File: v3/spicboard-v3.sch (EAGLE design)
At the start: 40 parts, among them IC1 74HC595, Q1 BC557, Q2 BC557

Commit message: SPiCboard...
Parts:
- C1, C2: device spicboard-v3:C2.5/2 -> capacitor-wima:C2.5/2
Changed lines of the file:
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@@
 <grid distance="0.1" unitdist="inch" unit="inch" style="lines" multiple="1" display="no" altdistance="0.01" altunitdist="inch" altunit="inch"/>
 <layers>
-<layer number="1" name="Top" color="4" fill="1" visible="yes" active="no"/>
-<layer number="16" name="Bottom" color="1" fill="1" visible="yes" active="no"/>
-<layer number="17" name="Pads" color="2" fill="1" visible="yes" active="no"/>
-<layer number="18" name="Vias" color="2" fill="1" visible="yes" active="no"/>
-<layer number="19" name="Unrouted" color="6" fill="1" visible="yes" active="no"/>
-<layer number="20" name="Dimension" color="15" fill="1" visible="yes" active="no"/>
-<layer number="21" name="tPlace" color="7" fill="1" visible="yes" active="no"/>
-<layer number="22" name="bPlace" color="7" fill="1" visible="yes" active="no"/>
-<layer number="23" name="tOrigins" color="15" fill="1" visible="yes" active="no"/>
-<layer number="24" name="bOrigins" color="15" fill="1" visible="yes" active="no"/>
-<layer number="25" name="tNames" color="7" fill="1" visible="yes" active="no"/>
-<layer number="26" name="bNames" color="7" fill="1" visible="yes" active="no"/>
-<layer number="27" name="tValues" color="7" fill="1" visible="yes" active="no"/>
-<layer number="28" name="bValues" color="7" fill="1" visible="yes" active="no"/>
+<layer number="1" name="Top" color="4" fill="1" visible="no" active="no"/>
+<layer number="16" name="Bottom" color="1" fill="1" visible="no" active="no"/>
+<layer number="17" name="Pads" color="2" fill="1" visible="no" active="no"/>
+<layer number="18" name="Vias" color="2" fill="1" visible="no" active="no"/>
+<layer number="19" name="Unrouted" color="6" fill="1" visible="no" active="no"/>
+<layer number="20" name="Dimension" color="15" fill="1" visible="no" active="no"/>
+<layer number="21" name="tPlace" color="7" fill="1" visible="no" active="no"/>
+<layer number="22" name="bPlace" color="7" fill="1" visible="no" active="no"/>
+<layer number="23" name="tOrigins" color="15" fill="1" visible="no" active="no"/>
+<layer number="24" name="bOrigins" color="15" fill="1" visible="no" active="no"/>
+<layer number="25" name="tNames" color="7" fill="1" visible="no" active="no"/>
+<layer number="26" name="bNames" color="7" fill="1" visible="no" active="no"/>
+<layer number="27" name="tValues" color="7" fill="1" visible="no" active="no"/>
+<layer number="28" name="bValues" color="7" fill="1" visible="no" active="no"/>
 <layer number="29" name="tStop" color="7" fill="3" visible="no" active="no"/>
 <layer number="30" name="bStop" color="7" fill="6" visible="no" active="no"/>
@@
 <layer number="35" name="tGlue" color="7" fill="4" visible="no" active="no"/>
 <layer number="36" name="bGlue" color="7" fill="5" visible="no" active="no"/>
-<layer number="37" name="tTest" color="7" fill="1" visible="yes" active="no"/>
-<layer number="38" name="bTest" color="7" fill="1" visible="yes" active="no"/>
+<layer number="37" name="tTest" color="7" fill="1" visible="no" active="no"/>
+<layer number="38" name="bTest" color="7" fill="1" visible="no" active="no"/>
 <layer number="39" name="tKeepout" color="4" fill="11" visible="no" active="no"/>
 <layer number="40" name="bKeepout" color="1" fill="11" visible="no" active="no"/>
@@
 <layer number="44" name="Drills" color="7" fill="1" visible="no" active="no"/>
 <layer number="45" name="Holes" color="7" fill="1" visible="no" active="no"/>
-<layer number="46" name="Milling" color="3" fill="1" visible="yes" active="no"/>
-<layer number="47" name="Measures" color="7" fill="1" visible="yes" active="no"/>
-<layer number="48" name="Document" color="7" fill="1" visible="yes" active="no"/>
-<layer number="49" name="Reference" color="7" fill="1" visible="yes" active="no"/>
-<layer number="50" name="dxf" color="7" fill="1" visible="yes" active="no"/>
-<layer number="51" name="tDocu" color="7" fill="1" visible="yes" active="no"/>
-<layer number="52" name="bDocu" color="7" fill="1" visible="yes" active="no"/>
-<layer number="53" name="tGND_GNDA" color="7" fill="9" visible="yes" active="no"/>
-<layer number="54" name="bGND_GNDA" color="1" fill="9" visible="yes" active="no"/>
-<layer number="56" name="wert" color="7" fill="1" visible="yes" active="no"/>
-<layer number="57" name="tCAD" color="7" fill="1" visible="yes" active="no"/>
-<layer number="59" name="tCarbon" color="7" fill="1" visible="yes" active="no"/>
-<layer number="60" name="bCarbon" color="7" fill="1" visible="yes" active="no"/>
+<layer number="46" name="Milling" color="3" fill="1" visible="no" active="no"/>
+<layer number="47" name="Measures" color="7" fill="1" visible="no" active="no"/>
+<layer number="48" name="Document" color="7" fill="1" visible="no" active="no"/>
+<layer number="49" name="Reference" color="7" fill="1" visible="no" active="no"/>
+<layer number="50" name="dxf" color="7" fill="1" visible="no" active="no"/>
+<layer number="51" name="tDocu" color="7" fill="1" visible="no" active="no"/>
+<layer number="52" name="bDocu" color="7" fill="1" visible="no" active="no"/>
+<layer number="53" name="tGND_GNDA" color="7" fill="9" visible="no" active="no"/>
+<layer number="54" name="bGND_GNDA" color="1" fill="9" visible="no" active="no"/>
+<layer number="56" name="wert" color="7" fill="1" visible="no" active="no"/>
+<layer number="57" name="tCAD" color="7" fill="1" visible="no" active="no"/>
+<layer number="59" name="tCarbon" color="7" fill="1" visible="no" active="no"/>
+<layer number="60" name="bCarbon" color="7" fill="1" visible="no" active="no"/>
 <layer number="90" name="Modules" color="5" fill="1" visible="yes" active="yes"/>
 <layer number="91" name="Nets" color="2" fill="1" visible="yes" active="yes"/>
@@
 <part name="R11" library="resistor" deviceset="R-EU_" device="0207/10" value="1k"/>
 <part name="P+7" library="supply1" deviceset="VCC" device=""/>
-<part name="C1" library="spicboard-v3" deviceset="C" device="2.5/2" value="100n"/>
+<part name="C1" library="capacitor-wima" deviceset="C" device="2.5/2" value="100n"/>
 <part name="P+8" library="supply1" deviceset="VCC" device=""/>
 <part name="GND6" library="supply1" deviceset="GND" device=""/>
 <part name="R12" library="resistor" deviceset="R-EU_" device="0207/10" value="1k"/>
-<part name="C2" library="spicboard-v3" deviceset="C" device="2.5/2" value="100n"/>
+<part name="C2" library="capacitor-wima" deviceset="C" device="2.5/2" value="100n"/>
 <part name="GND7" library="supply1" deviceset="GND" device=""/>
 <part name="R13" library="resistor" deviceset="R-EU_" device="0207/10" value="330"/>

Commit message: SPiCboard: PADs fertig
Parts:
- BLUE0, BLUE1, GREEN0, GREEN1, RED0, RED1, YELLOW0, YELLOW1: device led:LED5MM -> spicboard-v3:LED5MM
- C1, C2: device capacitor-wima:C2.5/2 -> spicboard-v3:C2.5/2
- R1, R10, R11, R12, R13, R14, R15, R2, R3, R4, R5, R6, R7, R8, R9: device resistor:R-EU_0207/10 -> spicboard-v3:R-EU_0207/10
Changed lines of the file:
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@@
 <parts>
 <part name="B1" library="spicboard-v3" deviceset="ARDUINO_UNO_R3_SHIELD" device="" value="ARDUINO_UNO_R3_SHIELD"/>
-<part name="RED0" library="led" deviceset="LED" device="5MM"/>
-<part name="YELLOW0" library="led" deviceset="LED" device="5MM"/>
-<part name="GREEN0" library="led" deviceset="LED" device="5MM"/>
-<part name="BLUE0" library="led" deviceset="LED" device="5MM"/>
-<part name="RED1" library="led" deviceset="LED" device="5MM"/>
-<part name="YELLOW1" library="led" deviceset="LED" device="5MM"/>
-<part name="GREEN1" library="led" deviceset="LED" device="5MM"/>
-<part name="BLUE1" library="led" deviceset="LED" device="5MM"/>
-<part name="R1" library="resistor" deviceset="R-EU_" device="0207/10" value="330"/>
-<part name="R2" library="resistor" deviceset="R-EU_" device="0207/10" value="330"/>
-<part name="R3" library="resistor" deviceset="R-EU_" device="0207/10" value="330"/>
-<part name="R4" library="resistor" deviceset="R-EU_" device="0207/10" value="10k"/>
-<part name="R5" library="resistor" deviceset="R-EU_" device="0207/10" value="330"/>
-<part name="R6" library="resistor" deviceset="R-EU_" device="0207/10" value="330"/>
-<part name="R7" library="resistor" deviceset="R-EU_" device="0207/10" value="330"/>
-<part name="R8" library="resistor" deviceset="R-EU_" device="0207/10" value="10k"/>
+<part name="RED0" library="spicboard-v3" deviceset="LED" device="5MM"/>
+<part name="YELLOW0" library="spicboard-v3" deviceset="LED" device="5MM"/>
+<part name="GREEN0" library="spicboard-v3" deviceset="LED" device="5MM"/>
+<part name="BLUE0" library="spicboard-v3" deviceset="LED" device="5MM"/>
+<part name="RED1" library="spicboard-v3" deviceset="LED" device="5MM"/>
+<part name="YELLOW1" library="spicboard-v3" deviceset="LED" device="5MM"/>
+<part name="GREEN1" library="spicboard-v3" deviceset="LED" device="5MM"/>
+<part name="BLUE1" library="spicboard-v3" deviceset="LED" device="5MM"/>
+<part name="R1" library="spicboard-v3" deviceset="R-EU_" device="0207/10" value="330"/>
+<part name="R2" library="spicboard-v3" deviceset="R-EU_" device="0207/10" value="330"/>
+<part name="R3" library="spicboard-v3" deviceset="R-EU_" device="0207/10" value="330"/>
+<part name="R4" library="spicboard-v3" deviceset="R-EU_" device="0207/10" value="10k"/>
+<part name="R5" library="spicboard-v3" deviceset="R-EU_" device="0207/10" value="330"/>
+<part name="R6" library="spicboard-v3" deviceset="R-EU_" device="0207/10" value="330"/>
+<part name="R7" library="spicboard-v3" deviceset="R-EU_" device="0207/10" value="330"/>
+<part name="R8" library="spicboard-v3" deviceset="R-EU_" device="0207/10" value="10k"/>
 <part name="IC1" library="74xx-eu" deviceset="74*595" device="N" technology="HC" value="74HC595"/>
 <part name="PHOTO" library="spicboard-v3" deviceset="LDR" device="" value="LDR"/>
@@
 <part name="GND2" library="supply1" deviceset="GND" device=""/>
 <part name="P+4" library="supply1" deviceset="VCC" device=""/>
-<part name="R10" library="resistor" deviceset="R-EU_" device="0207/10" value="49.9k"/>
+<part name="R10" library="spicboard-v3" deviceset="R-EU_" device="0207/10" value="49.9k"/>
 <part name="P+5" library="supply1" deviceset="VCC" device=""/>
 <part name="GND3" library="supply1" deviceset="GND" device=""/>
 <part name="P+6" library="supply1" deviceset="VCC" device=""/>
 <part name="GND4" library="supply1" deviceset="GND" device=""/>
-<part name="R9" library="resistor" deviceset="R-EU_" device="0207/10" value="1k"/>
-<part name="R11" library="resistor" deviceset="R-EU_" device="0207/10" value="1k"/>
+<part name="R9" library="spicboard-v3" deviceset="R-EU_" device="0207/10" value="1k"/>
+<part name="R11" library="spicboard-v3" deviceset="R-EU_" device="0207/10" value="1k"/>
 <part name="P+7" library="supply1" deviceset="VCC" device=""/>
-<part name="C1" library="capacitor-wima" deviceset="C" device="2.5/2" value="100n"/>
+<part name="C1" library="spicboard-v3" deviceset="C" device="2.5/2" value="100n"/>
 <part name="P+8" library="supply1" deviceset="VCC" device=""/>
 <part name="GND6" library="supply1" deviceset="GND" device=""/>
-<part name="R12" library="resistor" deviceset="R-EU_" device="0207/10" value="1k"/>
-<part name="C2" library="capacitor-wima" deviceset="C" device="2.5/2" value="100n"/>
+<part name="R12" library="spicboard-v3" deviceset="R-EU_" device="0207/10" value="1k"/>
+<part name="C2" library="spicboard-v3" deviceset="C" device="2.5/2" value="100n"/>
 <part name="GND7" library="supply1" deviceset="GND" device=""/>
-<part name="R13" library="resistor" deviceset="R-EU_" device="0207/10" value="330"/>
-<part name="R14" library="resistor" deviceset="R-EU_" device="0207/10" value="330"/>
+<part name="R13" library="spicboard-v3" deviceset="R-EU_" device="0207/10" value="330"/>
+<part name="R14" library="spicboard-v3" deviceset="R-EU_" device="0207/10" value="330"/>
 <part name="BTN0" library="switch-omron" deviceset="10-XX" device=""/>
 <part name="BTN1" library="switch-omron" deviceset="10-XX" device=""/>
@@
 <part name="OLED2" library="SparkFun-Connectors" deviceset="CONN_04" device=""/>
 <part name="COM" library="SparkFun-Connectors" deviceset="CONN_03" device=""/>
-<part name="R15" library="resistor" deviceset="R-EU_" device="0207/10" value="1k"/>
+<part name="R15" library="spicboard-v3" deviceset="R-EU_" device="0207/10" value="1k"/>
 <part name="P+9" library="supply1" deviceset="VCC" device=""/>
 <part name="EXT" library="SparkFun-Connectors" deviceset="CONN_03" device=""/>

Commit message: SPiCboard v3 ueberarbeitet
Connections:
- net MISO: no longer IC1A.QH*
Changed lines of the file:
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@@
 <segment>
 <pinref part="B1" gate="G$1" pin="D12"/>
-<wire x1="71.12" y1="33.02" x2="93.98" y2="33.02" width="0.1524" layer="91"/>
-<wire x1="93.98" y1="33.02" x2="93.98" y2="20.32" width="0.1524" layer="91"/>
-<wire x1="93.98" y1="20.32" x2="129.54" y2="20.32" width="0.1524" layer="91"/>
-<wire x1="129.54" y1="20.32" x2="129.54" y2="27.94" width="0.1524" layer="91"/>
-<pinref part="IC1" gate="A" pin="QH*"/>
-<wire x1="129.54" y1="27.94" x2="127" y2="27.94" width="0.1524" layer="91"/>
+<wire x1="71.12" y1="33.02" x2="78.74" y2="33.02" width="0.1524" layer="91"/>
 <label x="73.66" y="33.02" size="1.778" layer="95"/>
 </segment>

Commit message: SPiCboard: MISO + TODOs
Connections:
- net MISO: now also IC1A.QH*
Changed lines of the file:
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@@
 <segment>
 <pinref part="B1" gate="G$1" pin="D12"/>
-<wire x1="71.12" y1="33.02" x2="78.74" y2="33.02" width="0.1524" layer="91"/>
 <label x="73.66" y="33.02" size="1.778" layer="95"/>
+<wire x1="71.12" y1="33.02" x2="88.9" y2="33.02" width="0.1524" layer="91"/>
+<wire x1="88.9" y1="33.02" x2="88.9" y2="20.32" width="0.1524" layer="91"/>
+<wire x1="88.9" y1="20.32" x2="129.54" y2="20.32" width="0.1524" layer="91"/>
+<wire x1="129.54" y1="20.32" x2="129.54" y2="27.94" width="0.1524" layer="91"/>
+<pinref part="IC1" gate="A" pin="QH*"/>
+<wire x1="129.54" y1="27.94" x2="127" y2="27.94" width="0.1524" layer="91"/>
 </segment>
 </net>

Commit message: SPiCboard: 49.9k -> 30k, TODOs entfernt
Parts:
- R10: value 49.9k -> 30k
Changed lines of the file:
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@@
 <part name="GND2" library="supply1" deviceset="GND" device=""/>
 <part name="P+4" library="supply1" deviceset="VCC" device=""/>
-<part name="R10" library="spicboard-v3" deviceset="R-EU_" device="0207/10" value="49.9k"/>
+<part name="R10" library="spicboard-v3" deviceset="R-EU_" device="0207/10" value="30k"/>
 <part name="P+5" library="supply1" deviceset="VCC" device=""/>
 <part name="GND3" library="supply1" deviceset="GND" device=""/>

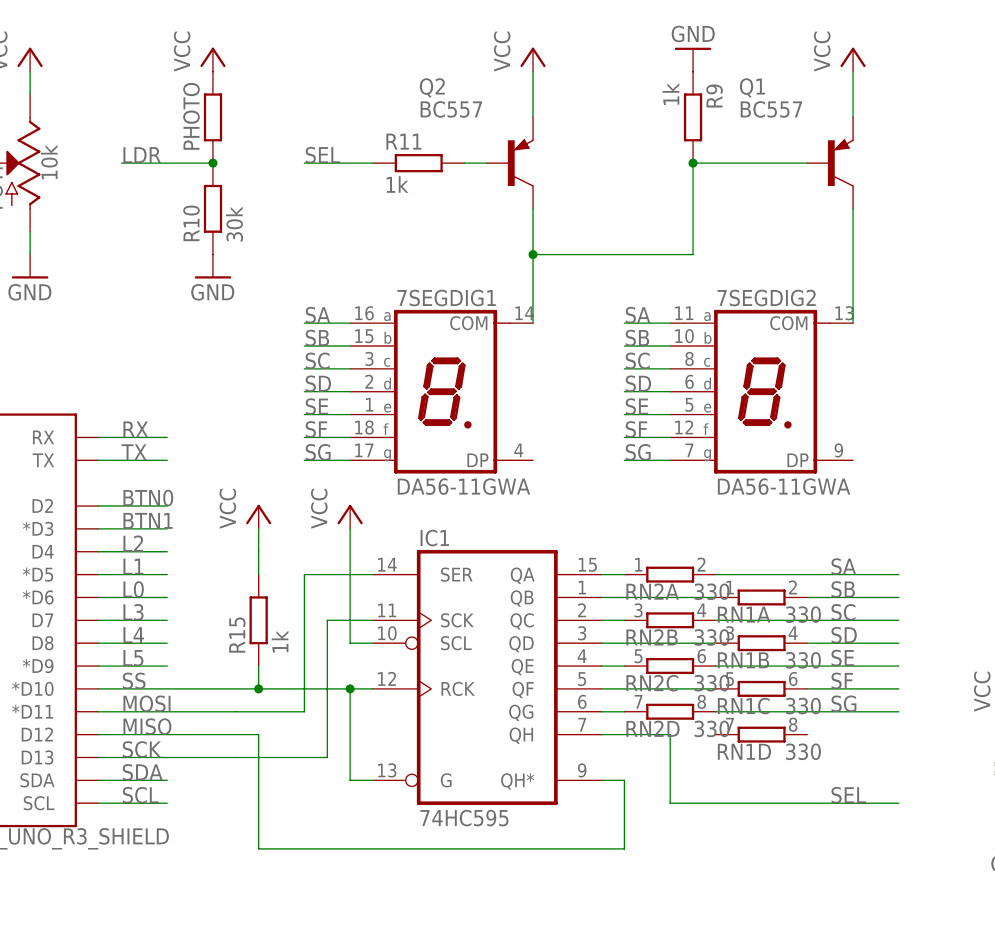
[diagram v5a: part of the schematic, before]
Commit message: SPiCboard v3: Photowiderstand durch Phototransistor ersetzt
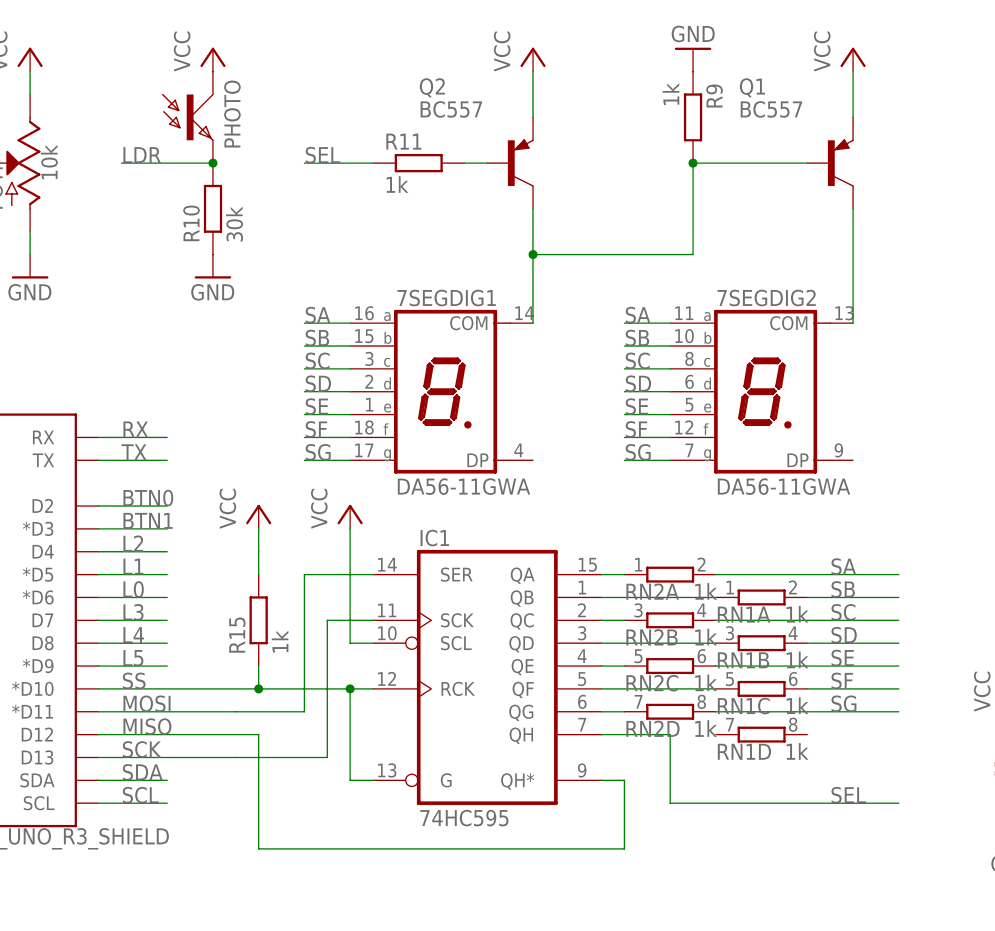
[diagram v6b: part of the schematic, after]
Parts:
- PHOTO: value LDR -> PTPT5MM; device spicboard-v3:LDR -> spicboard-v3:PTPT5MM
- RN1, RN2: value 330 -> 1k
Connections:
- net LDR: now also PHOTO.E; no longer PHOTO.1
- net VCC: now also PHOTO.C; no longer PHOTO.2
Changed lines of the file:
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@@
 <?xml version="1.0" encoding="utf-8"?>
 <!DOCTYPE eagle SYSTEM "eagle.dtd">
-<eagle version="8.0.0">
+<eagle version="8.1.0">
 <drawing>
 <settings>
@@
 <part name="R8" library="spicboard-v3" deviceset="R-EU_" device="0207/10" value="10k"/>
 <part name="IC1" library="74xx-eu" deviceset="74*595" device="N" technology="HC" value="74HC595"/>
-<part name="PHOTO" library="spicboard-v3" deviceset="LDR" device="" value="LDR"/>
 <part name="POTI" library="spicboard-v3" deviceset="POTENTIOMETER" device="-PTH-9MM-1/20W-20%" value="10k"/>
-<part name="RN1" library="spicboard-v3" deviceset="E4R" device="" value="330"/>
-<part name="RN2" library="spicboard-v3" deviceset="E4R" device="" value="330"/>
+<part name="RN1" library="spicboard-v3" deviceset="E4R" device="" value="1k"/>
+<part name="RN2" library="spicboard-v3" deviceset="E4R" device="" value="1k"/>
 <part name="Q1" library="transistor-pnp" deviceset="BC557*" device=""/>
 <part name="Q2" library="transistor-pnp" deviceset="BC557*" device=""/>
@@
 <part name="P+9" library="supply1" deviceset="VCC" device=""/>
 <part name="EXT" library="SparkFun-Connectors" deviceset="CONN_03" device=""/>
+<part name="PHOTO" library="spicboard-v3" deviceset="PT" device="PT5MM" value="PTPT5MM"/>
 </parts>
 <sheets>
@@
 <instance part="R8" gate="G$1" x="15.24" y="25.4"/>
 <instance part="IC1" gate="A" x="114.3" y="40.64"/>
-<instance part="PHOTO" gate="G$1" x="83.82" y="101.6" smashed="yes" rot="R90">
-<attribute name="NAME" x="82.3214" y="97.79" size="1.778" layer="95" rot="R90"/>
-</instance>
 <instance part="POTI" gate="G$1" x="63.5" y="96.52" rot="MR0"/>
 <instance part="RN1" gate="A" x="144.78" y="48.26"/>
@@
 <instance part="P+9" gate="VCC" x="88.9" y="58.42"/>
 <instance part="EXT" gate="J$1" x="45.72" y="-17.78" rot="R180"/>
+<instance part="PHOTO" gate="G$1" x="81.28" y="101.6" smashed="yes">
+<attribute name="NAME" x="86.868" y="98.044" size="1.778" layer="95" rot="R90"/>
+</instance>
 </instances>
 <busses>
@@
 <pinref part="P+4" gate="VCC" pin="VCC"/>
 <wire x1="63.5" y1="104.14" x2="63.5" y2="106.68" width="0.1524" layer="91"/>
-</segment>
-<segment>
-<pinref part="P+5" gate="VCC" pin="VCC"/>
-<pinref part="PHOTO" gate="G$1" pin="2"/>
 </segment>
 <segment>
@@
 <wire x1="88.9" y1="53.34" x2="88.9" y2="55.88" width="0.1524" layer="91"/>
 </segment>
+<segment>
+<pinref part="P+5" gate="VCC" pin="VCC"/>
+<pinref part="PHOTO" gate="G$1" pin="C"/>
+</segment>
 </net>
 <net name="GND" class="0">
@@
 <segment>
 <pinref part="R10" gate="G$1" pin="2"/>
-<pinref part="PHOTO" gate="G$1" pin="1"/>
 <wire x1="83.82" y1="96.52" x2="73.66" y2="96.52" width="0.1524" layer="91"/>
 <label x="73.66" y="96.52" size="1.778" layer="95"/>
+<pinref part="PHOTO" gate="G$1" pin="E"/>
 <junction x="83.82" y="96.52"/>
 </segment>
